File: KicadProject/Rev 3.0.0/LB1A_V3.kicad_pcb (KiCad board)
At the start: 6 copper layers, 45 x 45 mm, 194 parts, among them J601 2337019-1, J602 2337019-1, U101 LFBGA448_18X18, U201 AS4C256M16D3LC-12BCN, U401 STPMIC1xPQR, U501 S40FC004C1B2C00000, U601 LBEE59B1LV-278, U701 DF40C-100DP-0.4V(51), U702 DF40C-100DP-0.4V(51), U703 DF40C-100DP-0.4V(51), X101 32.768kHz, Y101 24MHz

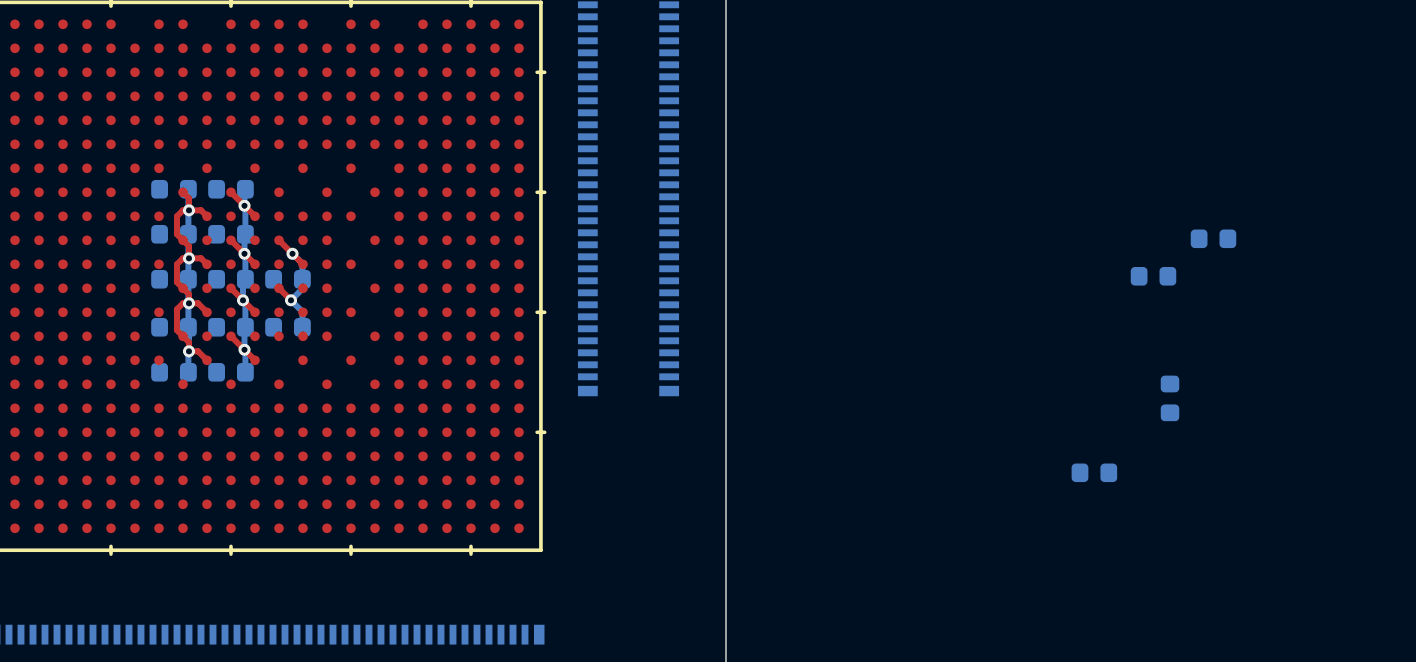
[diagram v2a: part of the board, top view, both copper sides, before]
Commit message: mcu vdd_core decoupling completed
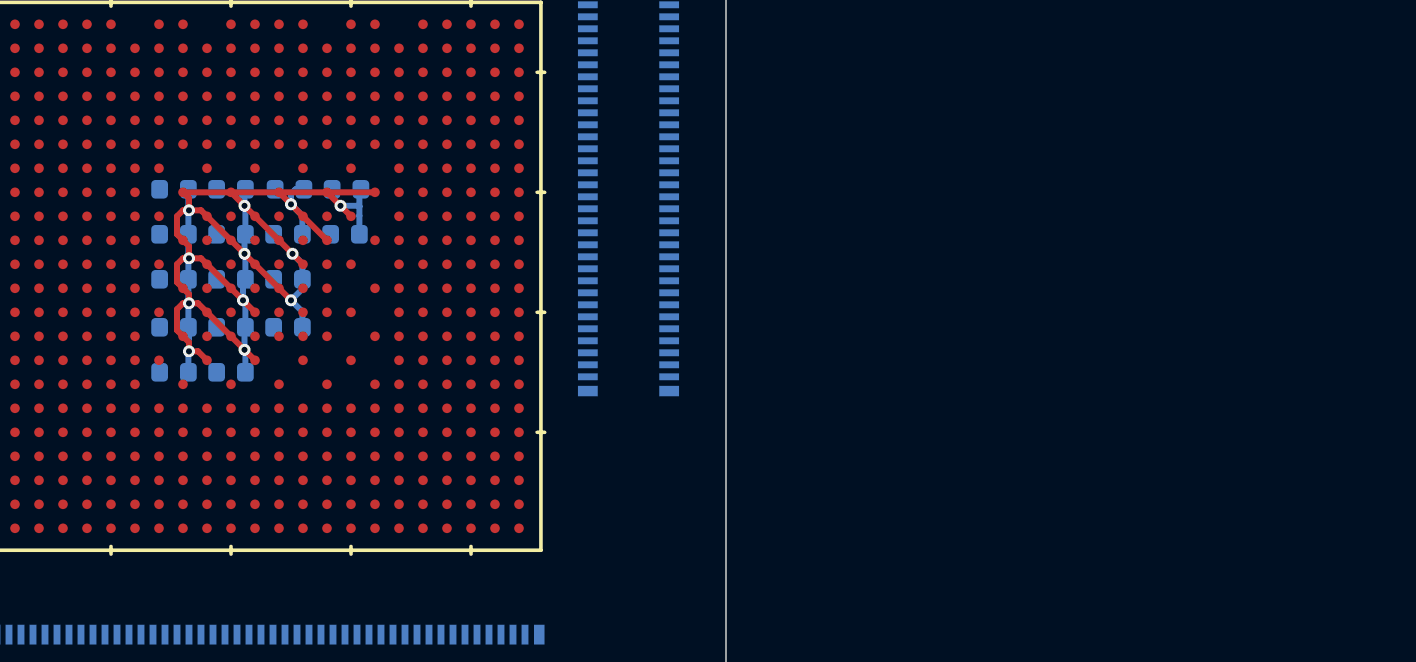
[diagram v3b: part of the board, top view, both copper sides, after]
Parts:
- moved C327 30.2 mm to (130.4, 110.8), turned to 180 degrees
- moved C329 28.9 mm to (132.3, 110.8), turned to 180 degrees
- moved C326 28.0 mm to (130.4, 112.3), turned to 180 degrees
- moved C328 27.0 mm to (132.3, 112.3), turned to 180 degrees
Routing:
- net PMIC_VOUT1_VDD_CORE: track 31.1 -> 50.7 mm, vias 10 -> 12
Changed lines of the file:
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@@
     (thickness 1.6)
     (drawings 8)
-    (tracks 87)
+    (tracks 114)
     (zones 0)
     (modules 194)
@@
   )
   (module U_Capacitor_SMD:C_0402_1005Metric (layer L6_Sig_Pwr.Cu)
-    (at 161.25 112.45)
+    (at 132.35 110.8 180)
     (descr "Capacitor SMD 0402 (1005 Metric), square (rectangular) end terminal, IPC_7351 nominal, (Body size source: IPC-SM-782 page 76, https://www.pcb-3d.com/wordpress/wp-content/uploads/ipc-sm-782a_amendment_1_and_2.pdf), generated with kicad-footprint-generator")
     (tags capacitor)
@@
       (effects (font (size 1 1) (thickness 0.15)) (justify mirror))
     )
+    (fp_line (start -0.91 -0.46) (end -0.91 0.46) (layer B.CrtYd) (width 0.05))
+    (fp_line (start -0.91 0.46) (end 0.91 0.46) (layer B.CrtYd) (width 0.05))
+    (fp_line (start 0.91 0.46) (end 0.91 -0.46) (layer B.CrtYd) (width 0.05))
+    (fp_line (start 0.91 -0.46) (end -0.91 -0.46) (layer B.CrtYd) (width 0.05))
     (fp_text user %R (at 0.13 -0.01) (layer B.Fab)
       (effects (font (size 0.5 0.5) (thickness 0.09)) (justify mirror))
     )
-    (fp_line (start 0.91 -0.46) (end -0.91 -0.46) (layer B.CrtYd) (width 0.05))
-    (fp_line (start 0.91 0.46) (end 0.91 -0.46) (layer B.CrtYd) (width 0.05))
-    (fp_line (start -0.91 0.46) (end 0.91 0.46) (layer B.CrtYd) (width 0.05))
-    (fp_line (start -0.91 -0.46) (end -0.91 0.46) (layer B.CrtYd) (width 0.05))
-    (pad 2 smd roundrect (at 0.48 0) (size 0.56 0.62) (layers L6_Sig_Pwr.Cu B.Paste B.Mask) (roundrect_rratio 0.25)
-      (net 1 GND))
-    (pad 1 smd roundrect (at -0.48 0) (size 0.56 0.62) (layers L6_Sig_Pwr.Cu B.Paste B.Mask) (roundrect_rratio 0.25)
+    (pad 1 smd roundrect (at -0.48 0 180) (size 0.56 0.62) (layers L6_Sig_Pwr.Cu B.Paste B.Mask) (roundrect_rratio 0.25)
       (net 11 PMIC_VOUT1_VDD_CORE))
+    (pad 2 smd roundrect (at 0.48 0 180) (size 0.56 0.62) (layers L6_Sig_Pwr.Cu B.Paste B.Mask) (roundrect_rratio 0.25)
+      (net 1 GND))
     (model ${KISYS3DMOD}/Capacitor_SMD.3dshapes/C_0402_1005Metric.wrl
       (at (xyz 0 0 0))
@@
   )
   (module U_Capacitor_SMD:C_0402_1005Metric (layer L6_Sig_Pwr.Cu)
-    (at 159.25 113.7)
+    (at 132.3 112.3 180)
     (descr "Capacitor SMD 0402 (1005 Metric), square (rectangular) end terminal, IPC_7351 nominal, (Body size source: IPC-SM-782 page 76, https://www.pcb-3d.com/wordpress/wp-content/uploads/ipc-sm-782a_amendment_1_and_2.pdf), generated with kicad-footprint-generator")
     (tags capacitor)
@@
     (fp_line (start -0.91 0.46) (end 0.91 0.46) (layer B.CrtYd) (width 0.05))
     (fp_line (start -0.91 -0.46) (end -0.91 0.46) (layer B.CrtYd) (width 0.05))
-    (pad 2 smd roundrect (at 0.48 0) (size 0.56 0.62) (layers L6_Sig_Pwr.Cu B.Paste B.Mask) (roundrect_rratio 0.25)
+    (pad 2 smd roundrect (at 0.48 0 180) (size 0.56 0.62) (layers L6_Sig_Pwr.Cu B.Paste B.Mask) (roundrect_rratio 0.25)
       (net 1 GND))
-    (pad 1 smd roundrect (at -0.48 0) (size 0.56 0.62) (layers L6_Sig_Pwr.Cu B.Paste B.Mask) (roundrect_rratio 0.25)
+    (pad 1 smd roundrect (at -0.48 0 180) (size 0.56 0.62) (layers L6_Sig_Pwr.Cu B.Paste B.Mask) (roundrect_rratio 0.25)
       (net 11 PMIC_VOUT1_VDD_CORE))
     (model ${KISYS3DMOD}/Capacitor_SMD.3dshapes/C_0402_1005Metric.wrl
@@
   )
   (module U_Capacitor_SMD:C_0402_1005Metric (layer L6_Sig_Pwr.Cu)
-    (at 159.8 117.77 90)
+    (at 130.45 110.8 180)
     (descr "Capacitor SMD 0402 (1005 Metric), square (rectangular) end terminal, IPC_7351 nominal, (Body size source: IPC-SM-782 page 76, https://www.pcb-3d.com/wordpress/wp-content/uploads/ipc-sm-782a_amendment_1_and_2.pdf), generated with kicad-footprint-generator")
     (tags capacitor)
     (attr smd)
-    (fp_text reference C327 (at 0 1.16 90) (layer B.SilkS) hide
+    (fp_text reference C327 (at 0 1.16) (layer B.SilkS) hide
       (effects (font (size 1 1) (thickness 0.15)) (justify mirror))
     )
-    (fp_text value 1uF (at 0 -1.16 90) (layer B.Fab) hide
+    (fp_text value 1uF (at 0 -1.16) (layer B.Fab) hide
       (effects (font (size 1 1) (thickness 0.15)) (justify mirror))
     )
-    (fp_text user %R (at 0.13 -0.01 90) (layer B.Fab)
+    (fp_text user %R (at 0.13 -0.01) (layer B.Fab)
       (effects (font (size 0.5 0.5) (thickness 0.09)) (justify mirror))
     )
@@
     (fp_line (start -0.91 0.46) (end 0.91 0.46) (layer B.CrtYd) (width 0.05))
     (fp_line (start -0.91 -0.46) (end -0.91 0.46) (layer B.CrtYd) (width 0.05))
-    (pad 2 smd roundrect (at 0.48 0 90) (size 0.56 0.62) (layers L6_Sig_Pwr.Cu B.Paste B.Mask) (roundrect_rratio 0.25)
+    (pad 2 smd roundrect (at 0.48 0 180) (size 0.56 0.62) (layers L6_Sig_Pwr.Cu B.Paste B.Mask) (roundrect_rratio 0.25)
       (net 1 GND))
-    (pad 1 smd roundrect (at -0.48 0 90) (size 0.56 0.62) (layers L6_Sig_Pwr.Cu B.Paste B.Mask) (roundrect_rratio 0.25)
+    (pad 1 smd roundrect (at -0.48 0 180) (size 0.56 0.62) (layers L6_Sig_Pwr.Cu B.Paste B.Mask) (roundrect_rratio 0.25)
       (net 11 PMIC_VOUT1_VDD_CORE))
     (model ${KISYS3DMOD}/Capacitor_SMD.3dshapes/C_0402_1005Metric.wrl
@@
   )
   (module U_Capacitor_SMD:C_0402_1005Metric (layer L6_Sig_Pwr.Cu)
-    (at 157.28 120.25)
+    (at 130.4 112.3 180)
     (descr "Capacitor SMD 0402 (1005 Metric), square (rectangular) end terminal, IPC_7351 nominal, (Body size source: IPC-SM-782 page 76, https://www.pcb-3d.com/wordpress/wp-content/uploads/ipc-sm-782a_amendment_1_and_2.pdf), generated with kicad-footprint-generator")
     (tags capacitor)
@@
     (fp_line (start -0.91 0.46) (end 0.91 0.46) (layer B.CrtYd) (width 0.05))
     (fp_line (start -0.91 -0.46) (end -0.91 0.46) (layer B.CrtYd) (width 0.05))
-    (pad 2 smd roundrect (at 0.48 0) (size 0.56 0.62) (layers L6_Sig_Pwr.Cu B.Paste B.Mask) (roundrect_rratio 0.25)
+    (pad 2 smd roundrect (at 0.48 0 180) (size 0.56 0.62) (layers L6_Sig_Pwr.Cu B.Paste B.Mask) (roundrect_rratio 0.25)
       (net 1 GND))
-    (pad 1 smd roundrect (at -0.48 0) (size 0.56 0.62) (layers L6_Sig_Pwr.Cu B.Paste B.Mask) (roundrect_rratio 0.25)
+    (pad 1 smd roundrect (at -0.48 0 180) (size 0.56 0.62) (layers L6_Sig_Pwr.Cu B.Paste B.Mask) (roundrect_rratio 0.25)
       (net 11 PMIC_VOUT1_VDD_CORE))
     (model ${KISYS3DMOD}/Capacitor_SMD.3dshapes/C_0402_1005Metric.wrl
@@
   (segment (start 130.88 114.12) (end 130.5 114.5) (width 0.2) (layer L6_Sig_Pwr.Cu) (net 11))
   (segment (start 130.88 113.8) (end 130.88 114.12) (width 0.2) (layer L6_Sig_Pwr.Cu) (net 11))
+  (via (at 130.5 111.3) (size 0.4) (drill 0.2) (layers L1_Sig_Pwr.Cu L6_Sig_Pwr.Cu) (net 11))
+  (segment (start 130.9 111.7) (end 130.5 111.3) (width 0.2) (layer L1_Sig_Pwr.Cu) (net 11))
+  (segment (start 130.1 110.9) (end 130.5 111.3) (width 0.2) (layer L1_Sig_Pwr.Cu) (net 11))
+  (segment (start 130.88 111.68) (end 130.5 111.3) (width 0.2) (layer L6_Sig_Pwr.Cu) (net 11))
+  (segment (start 130.88 112.3) (end 130.88 111.68) (width 0.2) (layer L6_Sig_Pwr.Cu) (net 11))
+  (segment (start 130.5 111.3) (end 130.5 110.95) (width 0.2) (layer L6_Sig_Pwr.Cu) (net 11))
+  (segment (start 130.65 110.8) (end 130.93 110.8) (width 0.2) (layer L6_Sig_Pwr.Cu) (net 11))
+  (segment (start 130.5 110.95) (end 130.65 110.8) (width 0.2) (layer L6_Sig_Pwr.Cu) (net 11))
+  (segment (start 132.5 111.7) (end 132.15 111.35) (width 0.2) (layer L1_Sig_Pwr.Cu) (net 11))
+  (segment (start 131.7 110.9) (end 132.15 111.35) (width 0.2) (layer L1_Sig_Pwr.Cu) (net 11))
+  (segment (start 132.78 112.3) (end 132.78 111.68) (width 0.2) (layer L6_Sig_Pwr.Cu) (net 11))
+  (segment (start 132.78 110.85) (end 132.83 110.8) (width 0.2) (layer L6_Sig_Pwr.Cu) (net 11))
+  (via (at 132.15 111.35) (size 0.4) (drill 0.2) (layers L1_Sig_Pwr.Cu L6_Sig_Pwr.Cu) (net 11))
+  (segment (start 132.15 111.35) (end 132.76 111.35) (width 0.2) (layer L6_Sig_Pwr.Cu) (net 11))
+  (segment (start 132.78 111.37) (end 132.78 110.85) (width 0.2) (layer L6_Sig_Pwr.Cu) (net 11))
+  (segment (start 132.76 111.35) (end 132.78 111.37) (width 0.2) (layer L6_Sig_Pwr.Cu) (net 11))
+  (segment (start 132.78 111.68) (end 132.78 111.37) (width 0.2) (layer L6_Sig_Pwr.Cu) (net 11))
+  (segment (start 126.9 110.9) (end 128.5 110.9) (width 0.2) (layer L1_Sig_Pwr.Cu) (net 11))
+  (segment (start 128.5 110.9) (end 130.1 110.9) (width 0.2) (layer L1_Sig_Pwr.Cu) (net 11))
+  (segment (start 130.1 110.9) (end 131.7 110.9) (width 0.2) (layer L1_Sig_Pwr.Cu) (net 11))
+  (segment (start 131.7 110.9) (end 133.3 110.9) (width 0.2) (layer L1_Sig_Pwr.Cu) (net 11))
+  (segment (start 128.5 115.7) (end 127.7 114.9) (width 0.2) (layer L1_Sig_Pwr.Cu) (net 11))
+  (segment (start 128.5 114.1) (end 127.7 113.3) (width 0.2) (layer L1_Sig_Pwr.Cu) (net 11))
+  (segment (start 128.5 112.5) (end 127.7 111.7) (width 0.2) (layer L1_Sig_Pwr.Cu) (net 11))
+  (segment (start 130.1 112.5) (end 129.3 111.7) (width 0.2) (layer L1_Sig_Pwr.Cu) (net 11))
+  (segment (start 130.1 114.1) (end 129.3 113.3) (width 0.2) (layer L1_Sig_Pwr.Cu) (net 11))
+  (segment (start 131.7 112.5) (end 130.9 111.7) (width 0.2) (layer L1_Sig_Pwr.Cu) (net 11))
   (zone (net 1) (net_name GND) (layer L2_Gnd.Cu) (hatch edge 0.508)
     (connect_pads yes (clearance 0.1))

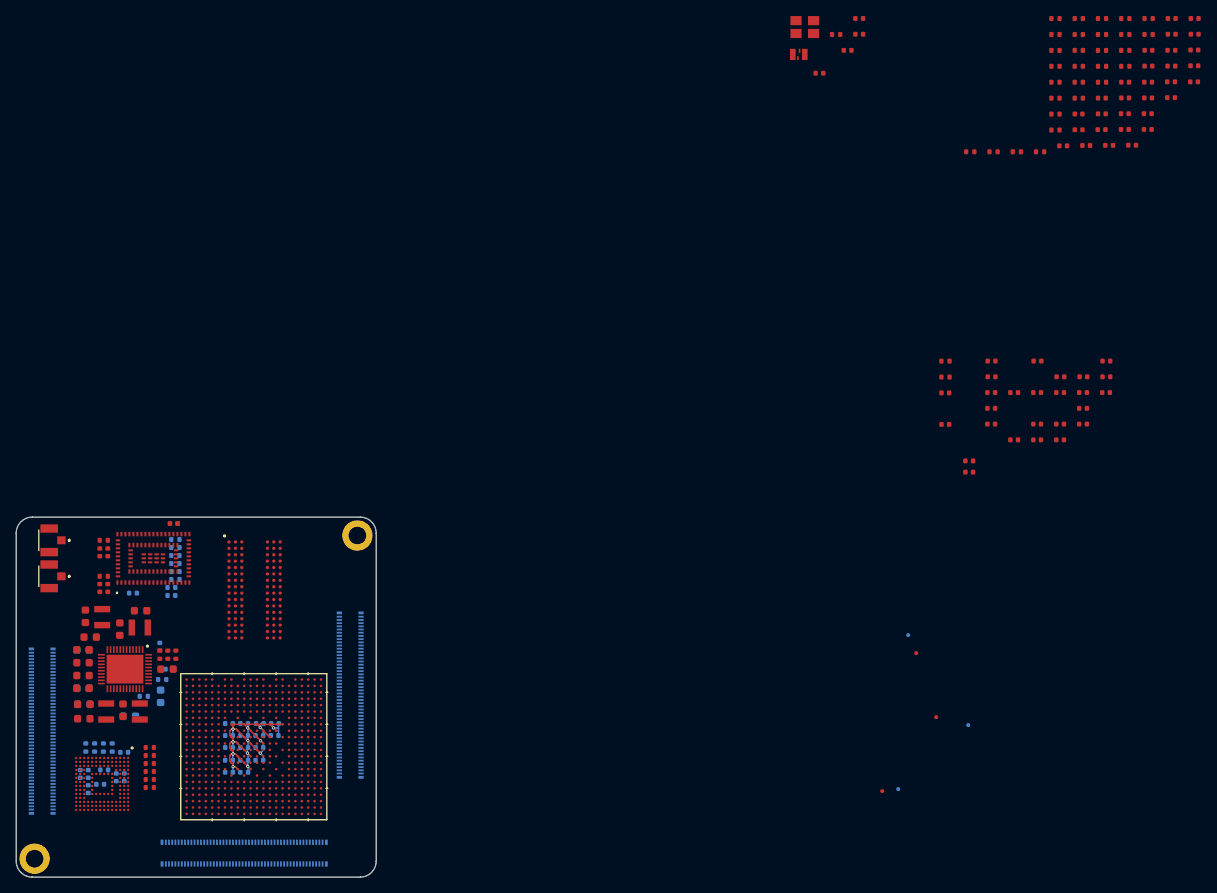
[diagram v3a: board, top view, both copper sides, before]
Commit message: mpu vdd complete
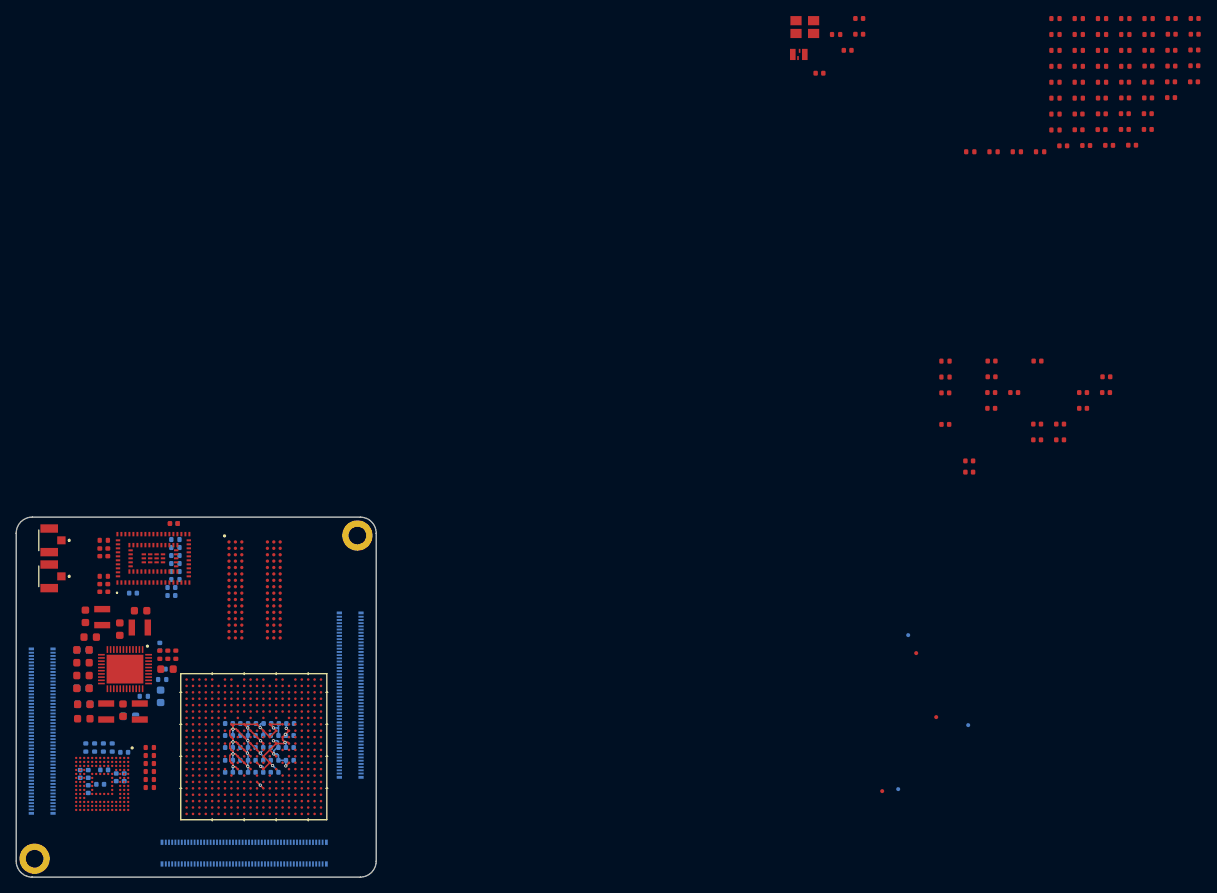
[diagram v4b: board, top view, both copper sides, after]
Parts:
- C301, C302, C303, C304, C309, C310, C311, C312: moved to B.Cu
- moved C301 117.7 mm to (130.4, 116.9), turned to 180 degrees
- moved C303 111.9 mm to (132.3, 115.4), turned to 180 degrees
- moved C304 107.7 mm to (132.3, 113.8), turned to 180 degrees
- moved C309 107.6 mm to (134.2, 115.4)
- moved C311 106.5 mm to (134.2, 112.3)
- moved C310 103.4 mm to (134.2, 113.8)
- moved C302 101.4 mm to (132.3, 116.9), turned to 180 degrees
- moved C312 95.3 mm to (134.2, 110.8)
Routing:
- net PMIC_VOUT3_VDD: track 0.00 -> 22.7 mm, vias 0 -> 9

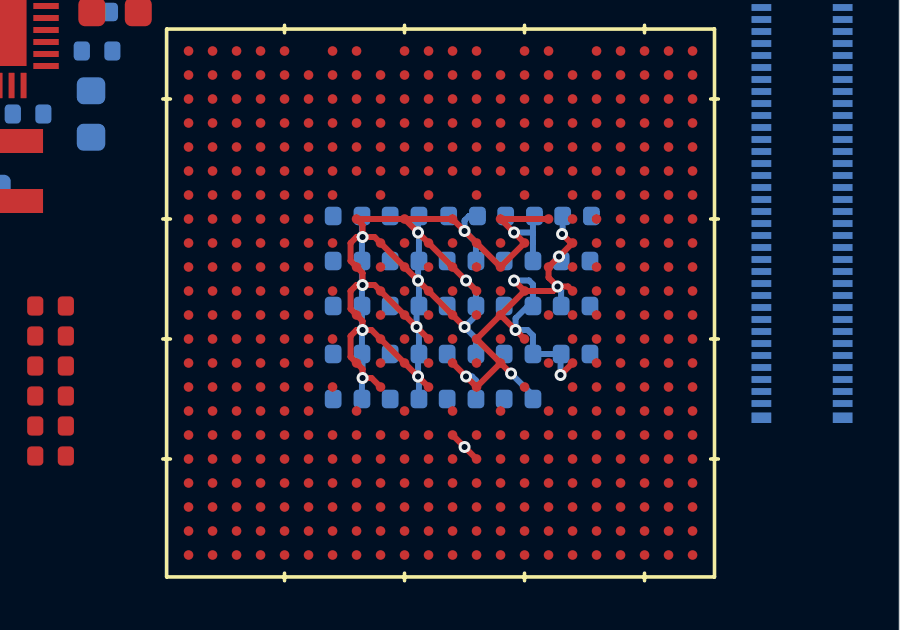
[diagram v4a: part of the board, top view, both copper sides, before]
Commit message: mpu connections
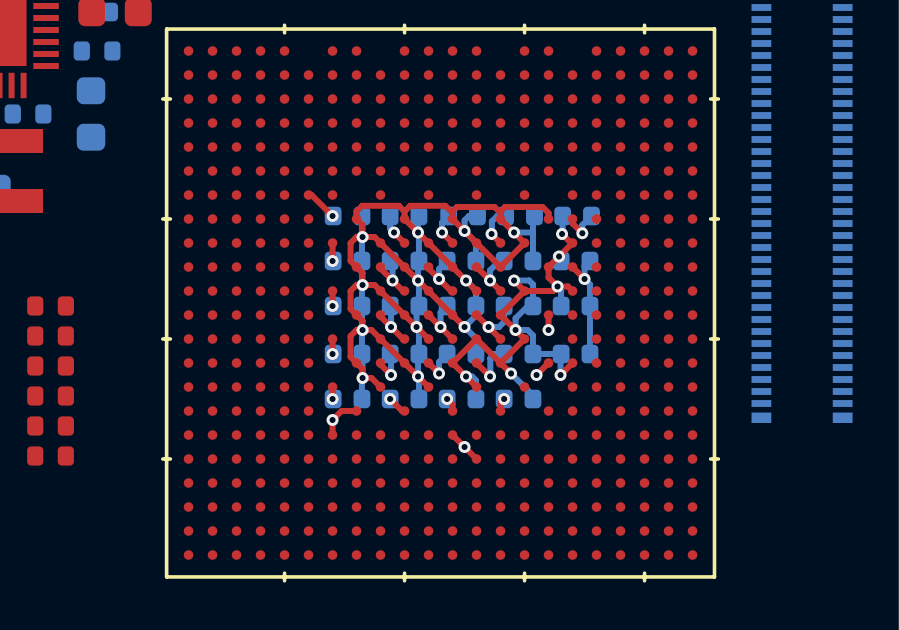
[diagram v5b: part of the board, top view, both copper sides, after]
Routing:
- net GND: track 0.00 -> 32.0 mm, vias 0 -> 25
- net PMIC_VOUT1_VDD_CORE: track 50.2 -> 54.0 mm
